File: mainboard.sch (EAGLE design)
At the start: 70 parts, among them T1 SINGLE_NCHAN_FET, T2 MOSFET_PCHAN_20A, T3 SINGLE_NCHAN_FET, T4 MOSFET_PCHAN_20A, T5 SINGLE_NCHAN_FET, T6 MOSFET_PCHAN_20A, U1 MURATA_REG_OKL-T3-W12, U2 TEENSY_3.0+4, U3 RFM23BP, U4 HMC5883LSMD, U5 ITG-3200, U6 AB0805, U7 CURRENT_MAX4372, U8 CURRENT_MAX4372, X1 CRYSTAL.ABS07

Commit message: Added stuff to mainboard for NanoRacks requirements
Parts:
- removed G1, G2, G3, G4, G5, G6: G125-FV20605L0P, G125-FV20605L0P:G125-FV20605L0P
- removed JP2, JP3, JP4, JP5, JP6, JP7: (no value), SparkFun-Connectors:M03X22X3_SILK_SM
- added C4: .1uF, SparkFun-Capacitors:CAP0805
- added J1: POWER_JACKPTH_LOCK, SparkFun-Connectors:POWER_JACKPTH_LOCK
- added JP1, JP10, JP11, JP12, JP8, JP9: (no value), SparkFun-Connectors:M03POLAR_LOCK
- added R12: 10K, SparkFun-Resistors:RESISTOR0805-RES
- added R13: 4.7K, SparkFun-Resistors:RESISTOR0805-RES
- added T7: MOSFET_PCHAN_20A, phonesat:MOSFET_PCHAN_20A
- added T8: SINGLE_NCHAN_FET, phonesat:SINGLE_NCHAN_FET
- R1: value 0R -> 3K3; device SparkFun-Resistors:RESISTOR2512 -> SparkFun-Resistors:RESISTOR0805-RES
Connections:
- new net ENAB_BURN4: R12.1, R13.2
- new net N$1: ST1.2, ST2.2, ST5.1
- new net N$8: C4.1, R12.2, T8.G
- new net N$9: R1.1, T7.G, T8.D
- new net VBURN4: T7.D@1, T7.D@2, T7.D@3, T7.D@4
- net BATT_INPUT: now also J1.PWR, ST1.1, ST2.1; no longer ST1.2, ST2.2
- net GND: now also C4.2, J1.GND, J1.GNDBREAK, JP1.1, JP10.1, JP11.1, JP12.1, JP8.1, JP9.1, R13.1, ST5.2, T8.S; no longer G1.P1, G1.P4, G2.P1, G2.P4, G3.P1, G3.P4, G4.P1, G4.P4, G5.P1, G5.P4, G6.P1, G6.P4, JP2.2, JP3.2, JP4.2, JP5.2, JP6.2, JP7.2, ST1.1, ST2.1, ST5.1
- net N$4: no longer R1.1
- net VBATT: no longer R1.2
- net VBURN1: now also JP1.3; no longer G4.P2, G4.P5
- net VBURN2: now also JP8.3; no longer G2.P2, G2.P5
- net VBURN3: now also JP9.3; no longer ST5.2
- net VBURN_IN: now also R1.2, T7.S@1, T7.S@2, T7.S@3
- net VSOLAR: now also JP1.2, JP10.2, JP11.2, JP12.2, JP8.2, JP9.2; no longer G1.P3, G1.P6, G2.P3, G2.P6, G3.P3, G3.P6, G4.P3, G4.P6, G5.P3, G5.P6, G6.P3, G6.P6
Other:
- note added: "BW4"
- note added: "Charging Jack"
- note added: "Rail Switch Connection"
- note removed: "Burn Wire 3 Terminal"
- note removed: "Option for 1 or 2 footswitches"

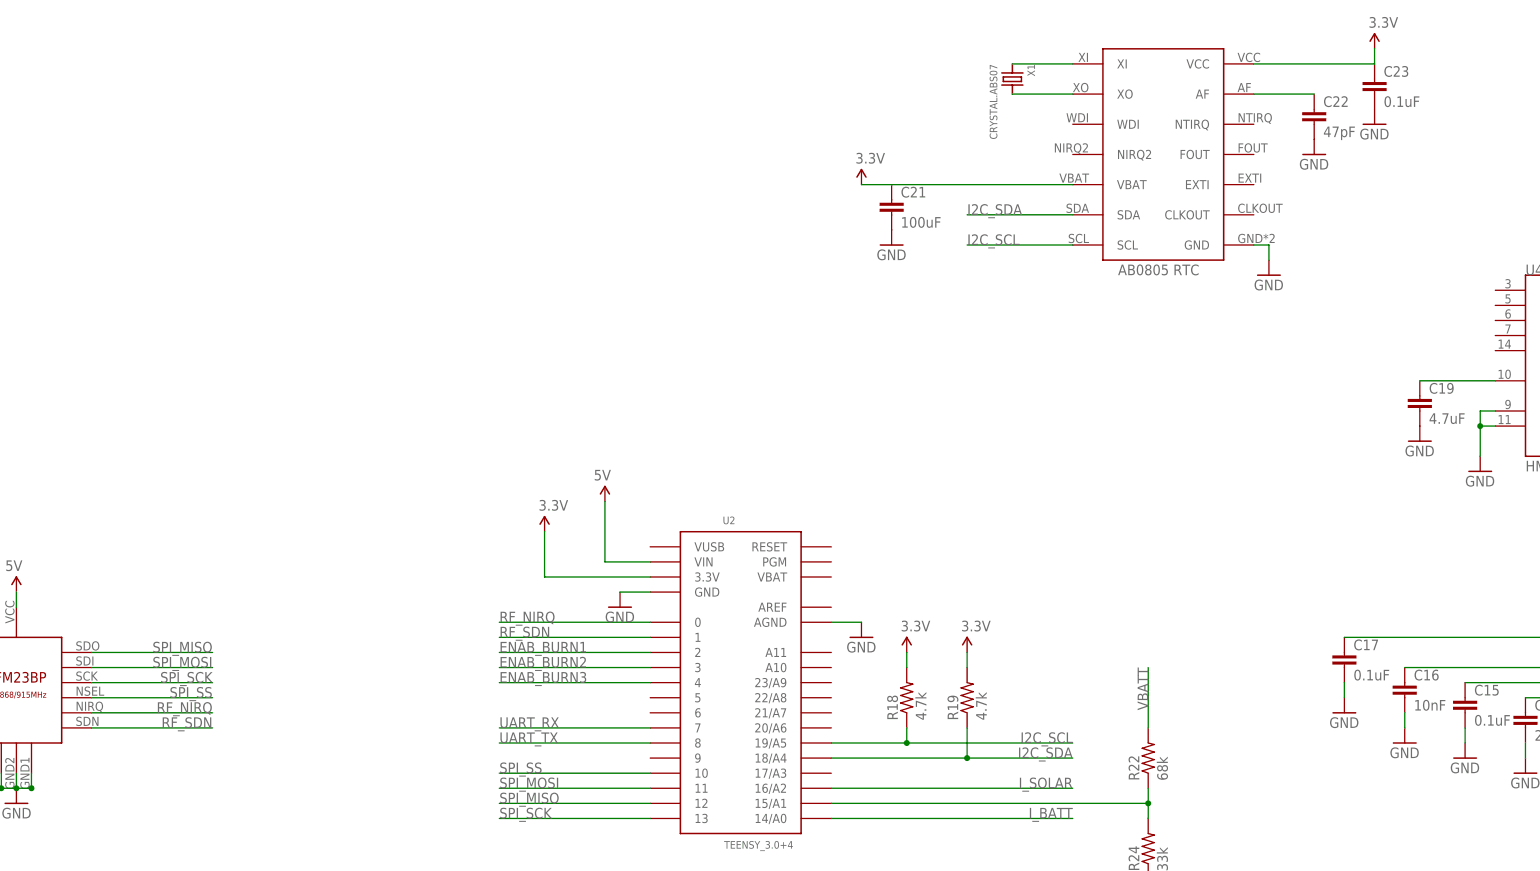
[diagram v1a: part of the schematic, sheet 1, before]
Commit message: Adding Arduino Pro Mini to Mainboard
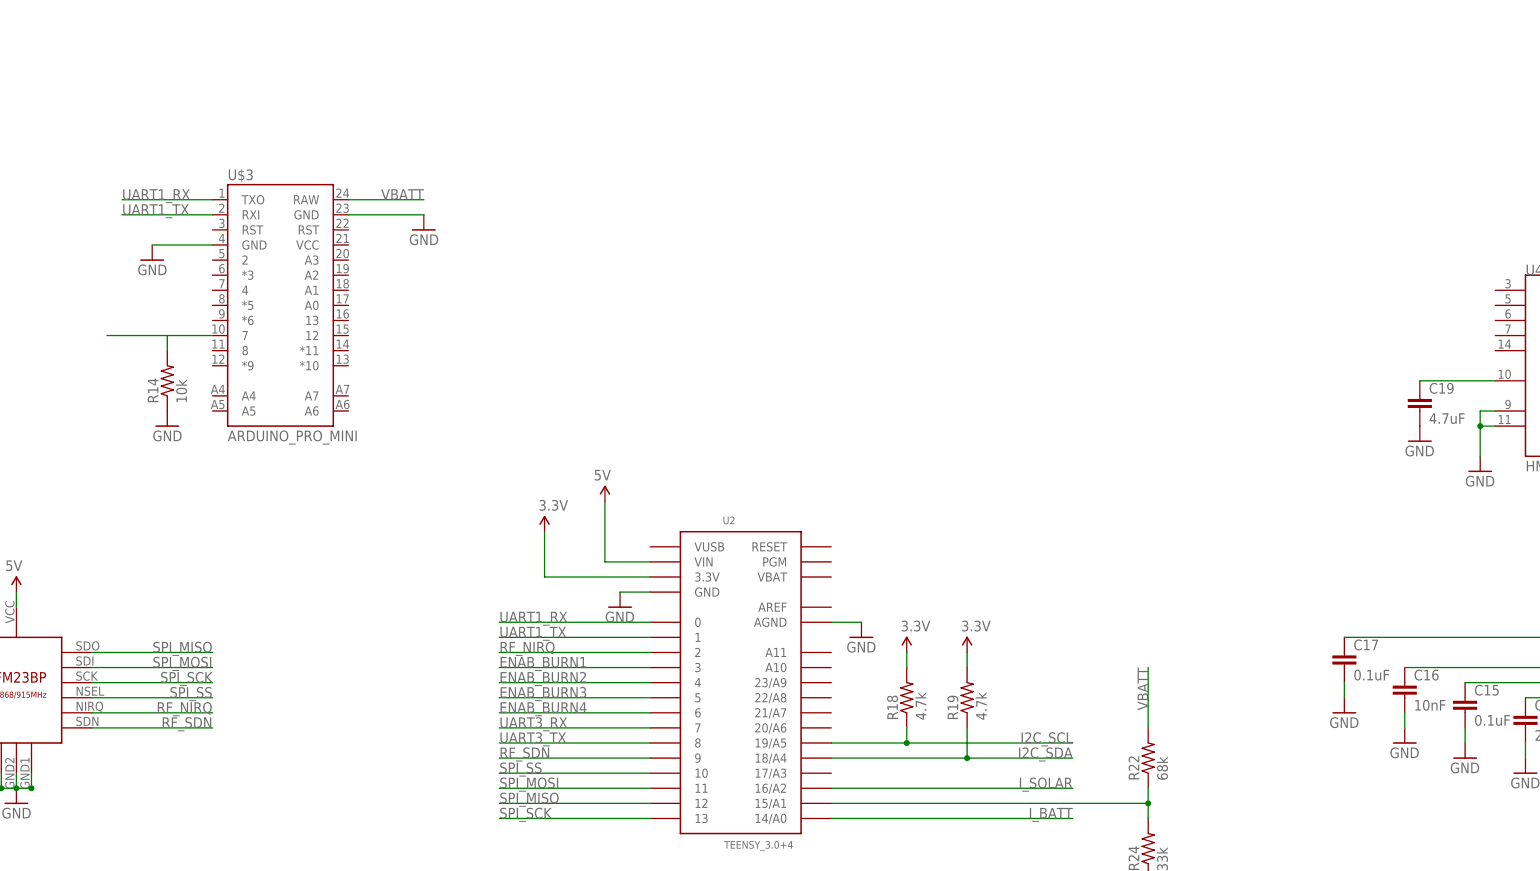
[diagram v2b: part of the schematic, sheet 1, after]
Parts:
- removed C21: 100uF, SparkFun-Capacitors:CAP1206
- removed C22: 47pF, SparkFun-Capacitors:CAP0805
- removed C23: 0.1uF, SparkFun-Capacitors:CAP0805
- removed U6: AB0805, AB0805:AB0805
- removed X1: CRYSTAL.ABS07, abracon:CRYSTAL.ABS07
- added R14: 10k, SparkFun-Resistors:RESISTOR0805-RES
- added U$3: ARDUINO_PRO_MINI, SparkFun-Boards:ARDUINO_PRO_MINI
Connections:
- net UART_RX renamed UART3_RX
- net UART_TX renamed UART3_TX
- removed net N$38: U6.XI, X1.1
- removed net N$41: U6.XO, X1.2
- removed net N$45: C22.1, U6.AF
- new net N$10: R14.2, U$3.7
- new net N_ENAB_REG: U1.ON/OFF
- new net UART1_RX: U$3.TXO, U2.0
- new net UART1_TX: U$3.RXI, U2.1
- net 3.3V: no longer C21.1, C23.1, U6.VBAT, U6.VCC
- net ENAB_BURN1: now also U2.3; no longer U2.2
- net ENAB_BURN2: now also U2.4; no longer U2.3
- net ENAB_BURN3: now also U2.5; no longer U2.4
- net ENAB_BURN4: now also U2.6
- net GND: now also R14.1, U$3.GND, U$3.GND@2; no longer C21.2, C22.2, C23.2, U1.ON/OFF, U6.GND
- net I2C_SCL: no longer U6.SCL
- net I2C_SDA: no longer U6.SDA
- net RF_NIRQ: now also U2.2; no longer U2.0
- net RF_SDN: now also U2.9; no longer U2.1
- net VBATT: now also U$3.RAW

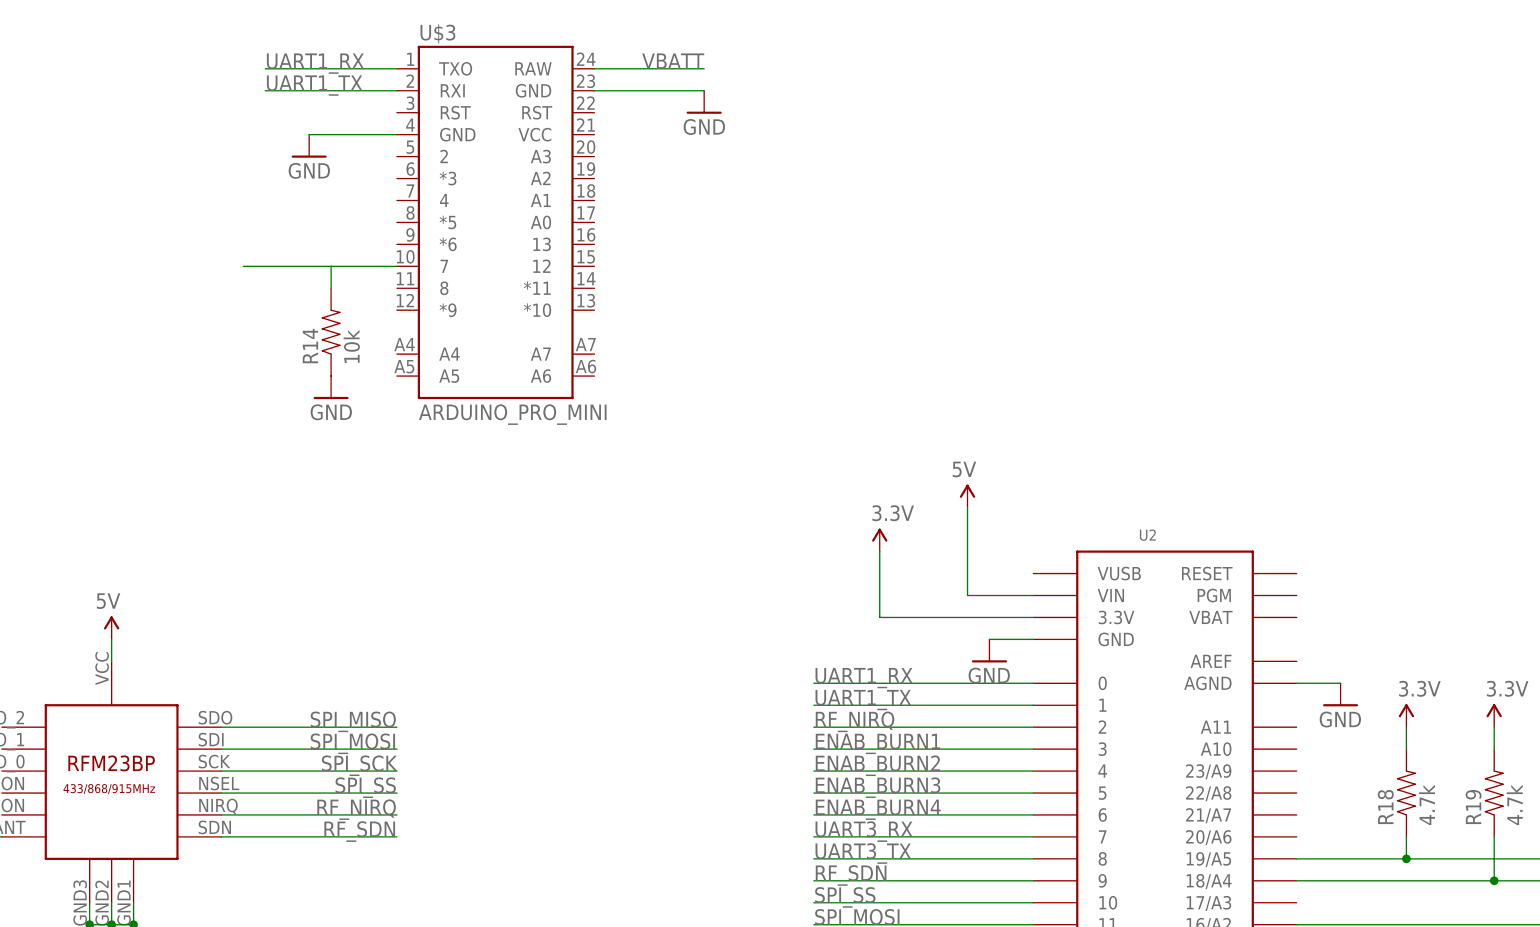
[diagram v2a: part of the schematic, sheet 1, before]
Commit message: Added switches for programming mode
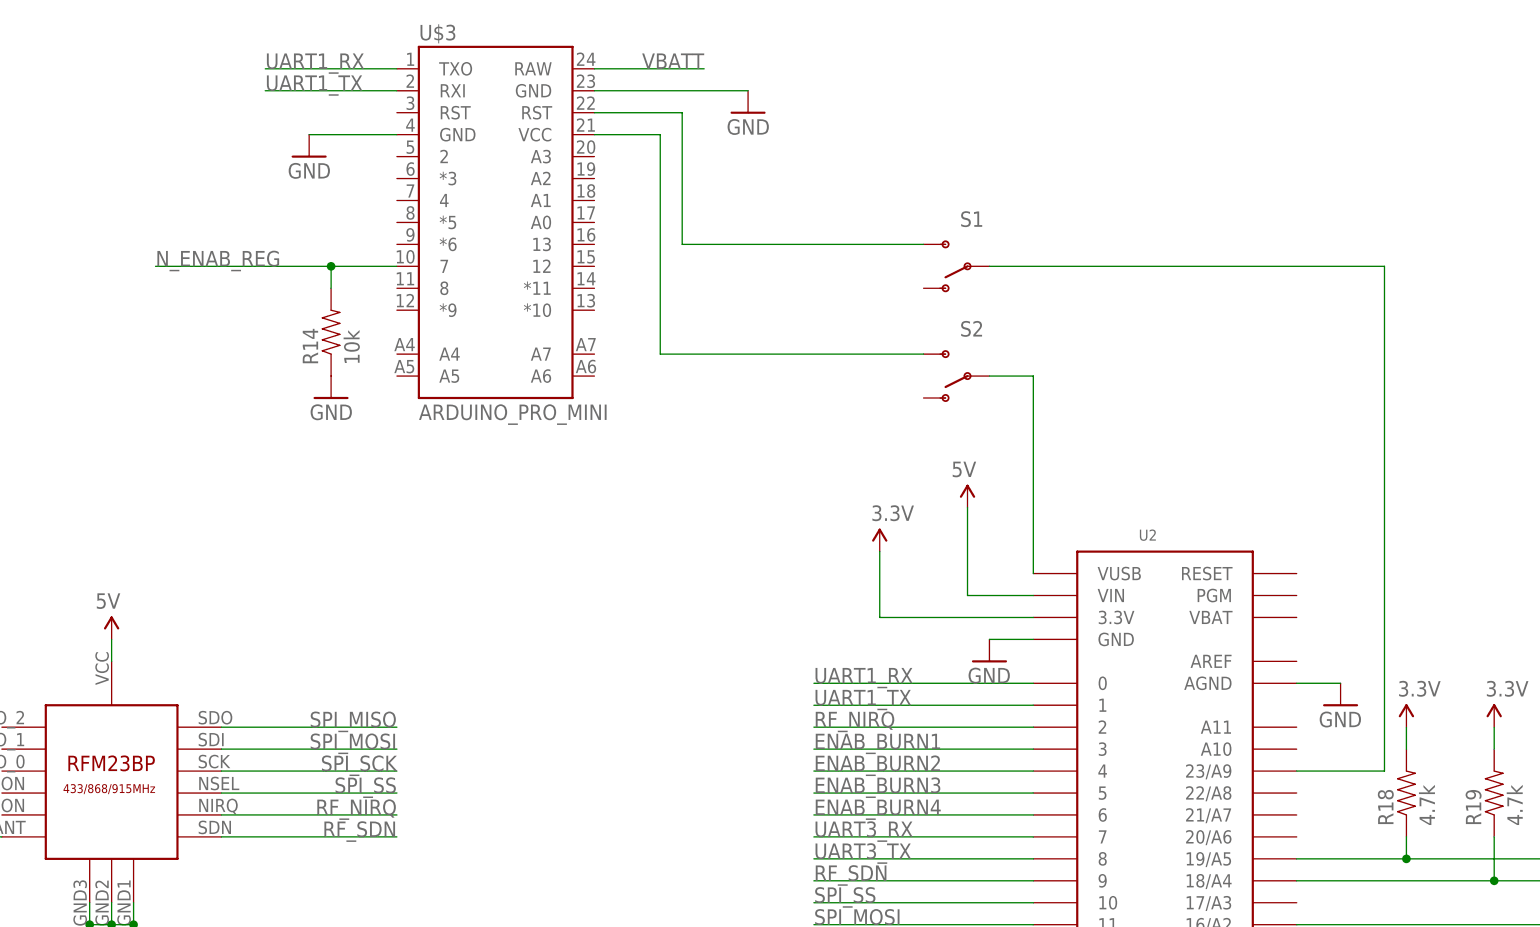
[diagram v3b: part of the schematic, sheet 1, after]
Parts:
- added S1, S2: (no value), SparkFun-Electromechanical:SWITCH-SPDTPTH
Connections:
- removed net N$10: R14.2, U$3.7
- new net N$11: S1.P, U2.23/A9
- new net N$13: S2.P, U2.VUSB
- new net PGM_RST: S1.S, U$3.RST@2
- new net PGM_VCC: S2.S, U$3.VCC
- net N_ENAB_REG: now also R14.2, U$3.7
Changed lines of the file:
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@@
 <part name="R14" library="SparkFun-Resistors" deviceset="RESISTOR" device="0805-RES" value="10k"/>
 <part name="GND19" library="SparkFun" deviceset="GND" device=""/>
+<part name="S1" library="SparkFun-Electromechanical" deviceset="SWITCH-SPDT" device="PTH"/>
+<part name="S2" library="SparkFun-Electromechanical" deviceset="SWITCH-SPDT" device="PTH"/>
 </parts>
 <sheets>
@@
 <instance part="P+3" gate="G$1" x="33.02" y="15.24"/>
 <instance part="SUPPLY1" gate="G$1" x="43.18" y="20.32" rot="MR0"/>
-<instance part="GND14" gate="1" x="12.7" y="66.04" rot="MR0"/>
+<instance part="GND14" gate="1" x="17.78" y="66.04" rot="MR0"/>
 <instance part="GND18" gate="1" x="-33.02" y="60.96" rot="MR0"/>
 <instance part="U$3" gate="G$1" x="-12.7" y="55.88"/>
 <instance part="R14" gate="G$1" x="-30.48" y="40.64" rot="R90"/>
 <instance part="GND19" gate="1" x="-30.48" y="33.02" rot="MR0"/>
+<instance part="S1" gate="1" x="43.18" y="48.26" rot="R180"/>
+<instance part="S2" gate="1" x="43.18" y="35.56" rot="R180"/>
 </instances>
 <busses>
@@
 <segment>
 <pinref part="GND14" gate="1" pin="GND"/>
-<wire x1="0" y1="68.58" x2="12.7" y2="68.58" width="0.1524" layer="91"/>
+<wire x1="0" y1="68.58" x2="17.78" y2="68.58" width="0.1524" layer="91"/>
 <pinref part="U$3" gate="G$1" pin="GND@2"/>
 </segment>
@@
 </segment>
 </net>
-<net name="N$10" class="0">
+<net name="N_ENAB_REG" class="0">
 <segment>
 <pinref part="U$3" gate="G$1" pin="7"/>
 <wire x1="-22.86" y1="48.26" x2="-30.48" y2="48.26" width="0.1524" layer="91"/>
 <wire x1="-30.48" y1="48.26" x2="-30.48" y2="45.72" width="0.1524" layer="91"/>
-<wire x1="-30.48" y1="48.26" x2="-40.64" y2="48.26" width="0.1524" layer="91"/>
+<wire x1="-30.48" y1="48.26" x2="-50.8" y2="48.26" width="0.1524" layer="91"/>
 <pinref part="R14" gate="G$1" pin="2"/>
-</segment>
-</net>
+<junction x="-30.48" y="48.26"/>
+<label x="-50.8" y="48.26" size="1.778" layer="95"/>
+</segment>
+</net>
+<net name="PGM_VCC" class="0">
+<segment>
+<pinref part="U$3" gate="G$1" pin="VCC"/>
+<wire x1="0" y1="63.5" x2="7.62" y2="63.5" width="0.1524" layer="91"/>
+<wire x1="7.62" y1="63.5" x2="7.62" y2="38.1" width="0.1524" layer="91"/>
+<pinref part="S2" gate="1" pin="S"/>
+<wire x1="38.1" y1="38.1" x2="7.62" y2="38.1" width="0.1524" layer="91"/>
+</segment>
+</net>
+<net name="N$11" class="0">
+<segment>
+<wire x1="91.44" y1="48.26" x2="91.44" y2="-10.16" width="0.1524" layer="91"/>
+<pinref part="U2" gate="G$1" pin="23/A9"/>
+<wire x1="91.44" y1="-10.16" x2="81.28" y2="-10.16" width="0.1524" layer="91"/>
+<pinref part="S1" gate="1" pin="P"/>
+<wire x1="45.72" y1="48.26" x2="91.44" y2="48.26" width="0.1524" layer="91"/>
+</segment>
+</net>
+<net name="PGM_RST" class="0">
+<segment>
+<pinref part="U$3" gate="G$1" pin="RST@2"/>
+<wire x1="0" y1="66.04" x2="10.16" y2="66.04" width="0.1524" layer="91"/>
+<wire x1="10.16" y1="66.04" x2="10.16" y2="50.8" width="0.1524" layer="91"/>
+<wire x1="10.16" y1="50.8" x2="38.1" y2="50.8" width="0.1524" layer="91"/>
+<pinref part="S1" gate="1" pin="S"/>
+</segment>
+</net>
+<net name="N$13" class="0">
+<segment>
+<pinref part="S2" gate="1" pin="P"/>
+<pinref part="U2" gate="G$1" pin="VUSB"/>
+<wire x1="45.72" y1="35.56" x2="50.8" y2="35.56" width="0.1524" layer="91"/>
+<wire x1="50.8" y1="35.56" x2="50.8" y2="12.7" width="0.1524" layer="91"/>
+</segment>
+</net>
